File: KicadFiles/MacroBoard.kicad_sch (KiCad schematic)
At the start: 76 parts, among them J1 USB_B_Micro, J2 Conn_01x08_Male, J3 Conn_01x24_Female, SW1 SW_Push, SW10 SW_Push, SW11 SW_Push, SW12 SW_Push, SW13 RotaryEncoder_Switch, SW14 SW_Push, SW15 SW_Push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

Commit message: Add files via upload
TODO: 
add footprints
add pads for measurments
create PCB design
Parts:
- removed C27, C28, C29: 4.7u, symbol Device:C
- removed J3: Conn_01x24_Female, symbol Connector:Conn_01x24_Female
- removed U2: IFX27001TFV, Package_TO_SOT_SMD:TO-252-3_TabPin2, symbol Regulator_Linear:IFX27001TFV
- added D18: LED_RAGB, symbol Device:LED_RAGB
- added R8: 100, symbol Device:R
- added R9: 150, symbol Device:R
- added U2: TC1262-33, symbol Regulator_Linear:TC1262-33
- C25, C26: value C -> 1u
- R6: value 1M -> 100
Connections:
- net +3V3: now also U2.3 (VO)
- net +5V: now also D18.2 (A), U2.1 (VI)
- net GND: now also U2.2 (GND); no longer R6.2
- net led_blue: now reaches R6.1
- net led_blue: now also U1.31 (PA10)
- net led_green: now reaches U1.32 (PA11)
- net led_green: now also R8.1
- net CS: no longer names the net of U1.26 (PB13)
- net D/C: no longer names the net of U1.28 (PB15)
- net MISO renamed led_red
- net led_red: now also R9.1
- net MOSI: no longer names the net of U1.41 (PB5)
- net RES: no longer names the net of U1.27 (PB14)
- new net: D18.1 (RK), R9.2
- new net: D18.3 (GK), R8.2
- new net: D18.4 (BK), R6.2
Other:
- note added: "0.2"
- note added: "15.12.2022r."
- note added: "DNP"
- note added: "NOTES: - all resistors 1/4W unless specified - switch capacitors - DNP - JTAG connector for programming - DNP"
- note added: "RGB LED"
- note added: "TC1263 used"
- note added: "TODO: - footprint assignment - add pads for measurments"
- note removed: "0.1"
- note removed: "26.11.2022r."
- note removed: "OLED connector"
- note removed: "TODO: find the right voltage regulator and capacitor sizes"
- note removed: "change to the desired IC"

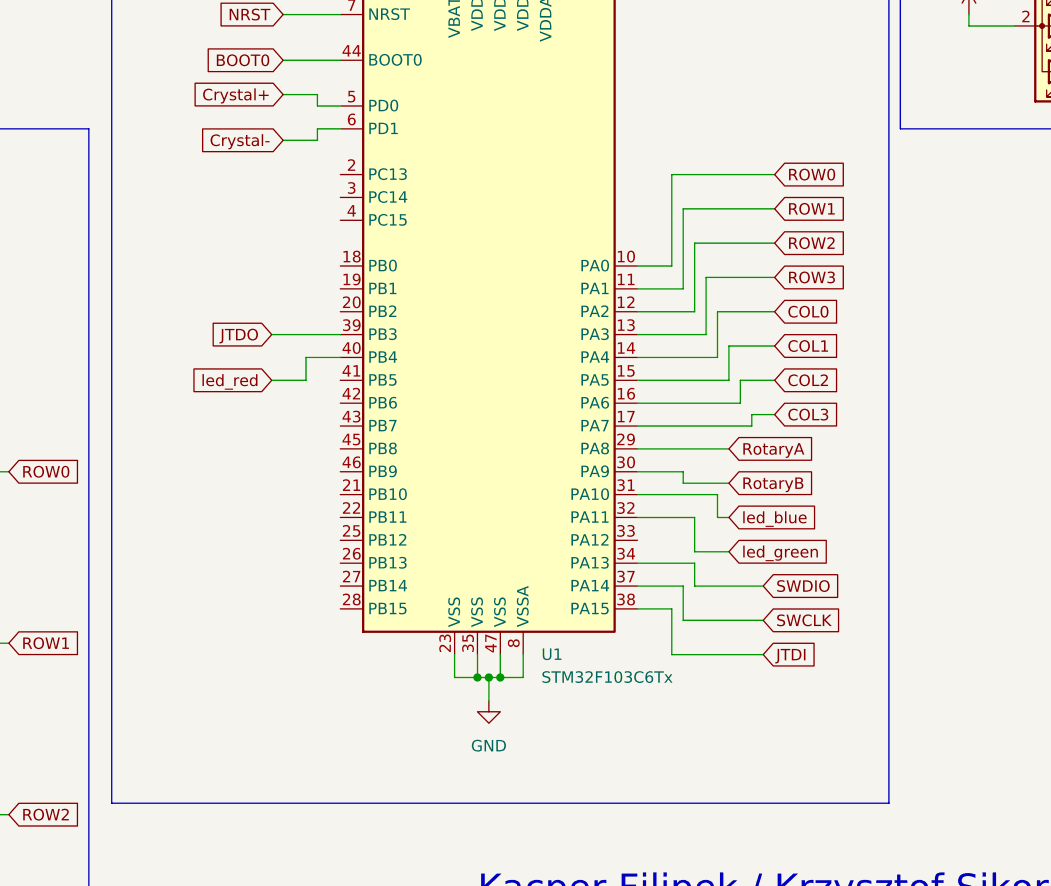
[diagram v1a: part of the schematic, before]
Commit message: Add files via upload
Pinout changes
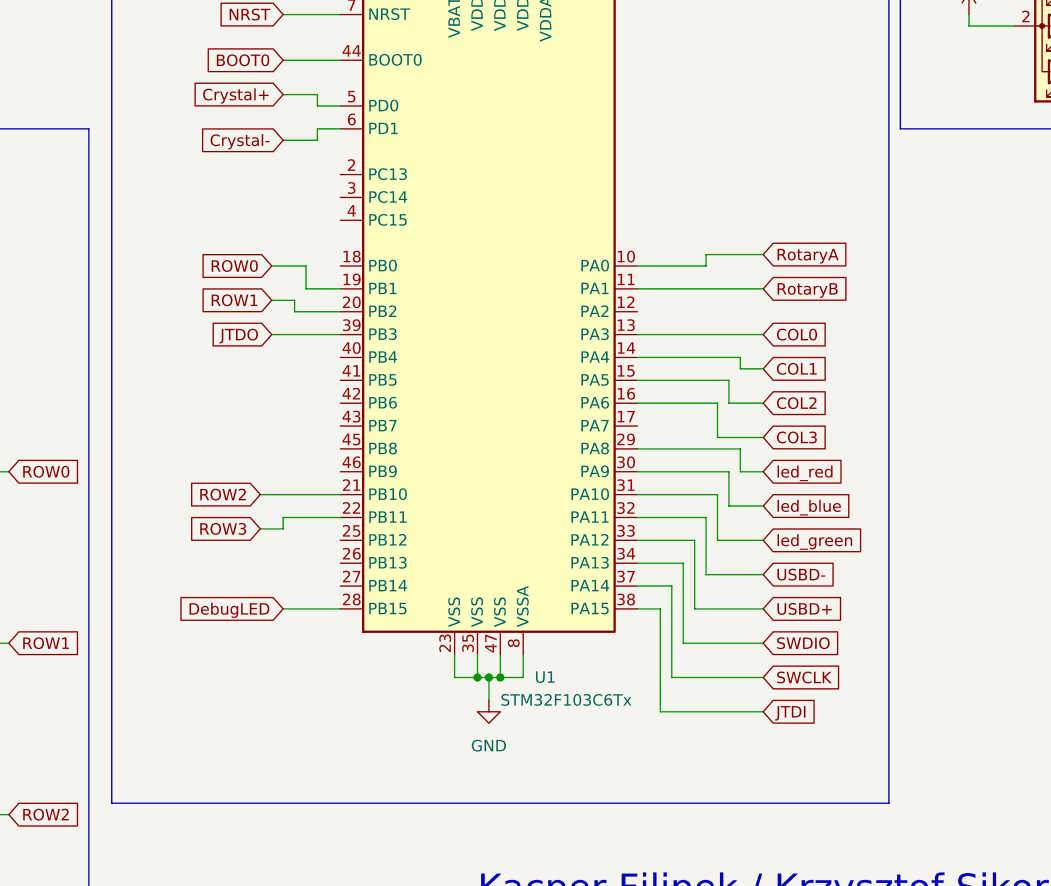
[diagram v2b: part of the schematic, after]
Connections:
- net COL0: now also U1.13 (PA3); no longer U1.14 (PA4)
- net COL1: now also U1.14 (PA4); no longer U1.15 (PA5)
- net COL2: now also U1.15 (PA5); no longer U1.16 (PA6)
- net COL3: now also U1.16 (PA6); no longer U1.17 (PA7)
- net DebugLED: now also U1.28 (PB15)
- net ROW0: now also U1.19 (PB1); no longer U1.10 (PA0)
- net ROW1: now also U1.20 (PB2); no longer U1.11 (PA1)
- net ROW2: now also U1.21 (PB10); no longer U1.12 (PA2)
- net ROW3: now also U1.22 (PB11); no longer U1.13 (PA3)
- net RotaryA: now also U1.10 (PA0); no longer U1.29 (PA8)
- net RotaryB: now also U1.11 (PA1); no longer U1.30 (PA9)
- net USBD+: now also U1.33 (PA12)
- net USBD-: now also U1.32 (PA11)
- net led_blue: now also U1.30 (PA9); no longer U1.31 (PA10)
- net led_green: now also U1.31 (PA10); no longer U1.32 (PA11)
- net led_red: now also U1.29 (PA8); no longer U1.40 (PB4)

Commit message: schematic done
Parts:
- added H1, H2, H3, H4: MountingHole, MountingHole:MountingHole_3mm, symbol Mechanical:MountingHole
- C1, C2: footprint (none) -> Capacitor_SMD:C_0603_1608Metric_Pad1.08x0.95mm_HandSolder
- C10, C11, C12, C13, C14, C15, C16, C17, C18, C19, C20, C21, C22, C23, C24, C25, C26, C3, C4, C5, C6, C7, C8, C9: footprint (none) -> Capacitor_SMD:C_0805_2012Metric_Pad1.18x1.45mm_HandSolder
- D1, D10, D11, D12, D13, D14, D15, D16, D2, D3, D4, D5, D6, D7, D8, D9: footprint (none) -> Diode_SMD:D_SOD-123F
- D17: footprint (none) -> LED_THT:LED_D5.0mm
- D18: footprint (none) -> LED_SMD:LED_SK6812_PLCC4_5.0x5.0mm_P3.2mm
- J1: footprint Connector_USB:USB_Micro-B_Molex_47346-0001 -> Connector_USB:USB_Micro-AB_Molex_47590-0001
- J2: footprint (none) -> Connector_PinHeader_2.54mm:PinHeader_1x08_P2.54mm_Horizontal
- R1, R2, R3, R4, R5, R6, R7, R8, R9: footprint (none) -> Resistor_SMD:R_1206_3216Metric_Pad1.30x1.75mm_HandSolder
- SW1, SW10, SW11, SW12, SW14, SW15, SW16, SW17, SW2, SW3, SW4, SW5, SW6, SW7, SW8, SW9: footprint (none) -> Button_Switch_Keyboard:SW_Cherry_MX_1.00u_PCB
- SW13: footprint (none) -> Rotary_Encoder:RotaryEncoder_Alps_EC11E-Switch_Vertical_H20mm
- U2: footprint (none) -> Package_SO:PowerIntegrations_SO-8
- Y1: footprint (none) -> Crystal:Crystal_SMD_HC49-SD_HandSoldering
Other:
- note added: "18.12.2022r."
- note added: "TODO: - add pads for measurments"
- note added: "keep those caps close to individual uC pins"
- note added: "mounting holes"
- note removed: "15.12.2022r."
- note removed: "TODO: - footprint assignment - add pads for measurments"
- note removed: "keep caps close to uC"

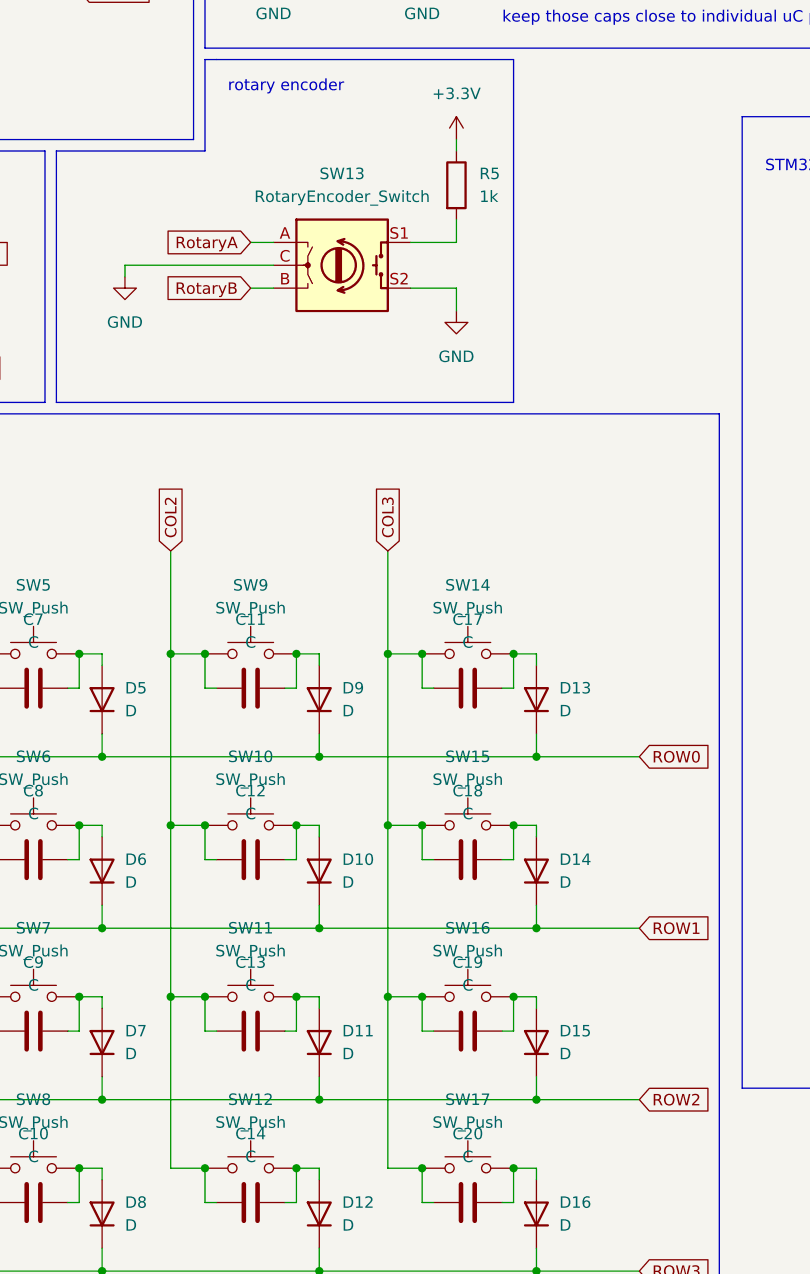
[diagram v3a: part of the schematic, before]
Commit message: pcb: arranged and connected switches with caps and diodes, everything else sucks
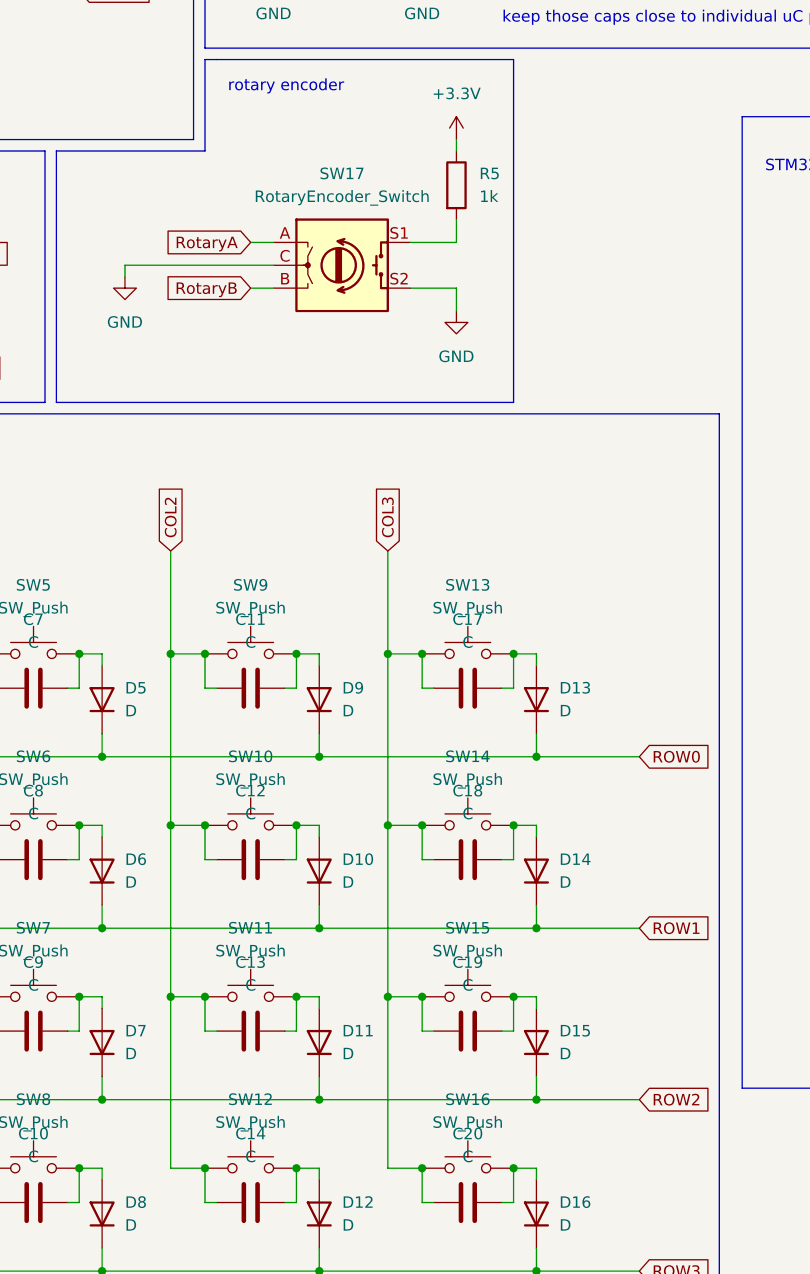
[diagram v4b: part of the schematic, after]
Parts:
- renumbered SW14 to SW13, SW15 to SW14, SW16 to SW15, SW17 to SW16, SW13 to SW17
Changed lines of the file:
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@@
   (symbol (lib_id "Switch:SW_Push") (at 106.68 111.76 0) (unit 1)
     (in_bom yes) (on_board yes) (fields_autoplaced)
-    (property "Reference" "SW14" (id 0) (at 106.68 104.14 0))
+    (property "Reference" "SW13" (id 0) (at 106.68 104.14 0))
     (property "Value" "SW_Push" (id 1) (at 106.68 106.68 0))
     (property "Footprint" "Button_Switch_Keyboard:SW_Cherry_MX_1.00u_PCB" (id 2) (at 106.68 106.68 0)
@@
   (symbol (lib_id "Switch:SW_Push") (at 106.68 149.86 0) (unit 1)
     (in_bom yes) (on_board yes) (fields_autoplaced)
-    (property "Reference" "SW16" (id 0) (at 106.68 142.24 0))
+    (property "Reference" "SW15" (id 0) (at 106.68 142.24 0))
     (property "Value" "SW_Push" (id 1) (at 106.68 144.78 0))
     (property "Footprint" "Button_Switch_Keyboard:SW_Cherry_MX_1.00u_PCB" (id 2) (at 106.68 144.78 0)
@@
   (symbol (lib_id "Switch:SW_Push") (at 106.68 168.91 0) (unit 1)
     (in_bom yes) (on_board yes) (fields_autoplaced)
-    (property "Reference" "SW17" (id 0) (at 106.68 161.29 0))
+    (property "Reference" "SW16" (id 0) (at 106.68 161.29 0))
     (property "Value" "SW_Push" (id 1) (at 106.68 163.83 0))
     (property "Footprint" "Button_Switch_Keyboard:SW_Cherry_MX_1.00u_PCB" (id 2) (at 106.68 163.83 0)
@@
   (symbol (lib_id "Device:RotaryEncoder_Switch") (at 92.71 68.58 0) (unit 1)
     (in_bom yes) (on_board yes)
-    (property "Reference" "SW13" (id 0) (at 92.71 58.42 0))
+    (property "Reference" "SW17" (id 0) (at 92.71 58.42 0))
     (property "Value" "RotaryEncoder_Switch" (id 1) (at 92.71 60.96 0))
     (property "Footprint" "Rotary_Encoder:RotaryEncoder_Alps_EC11E-Switch_Vertical_H20mm" (id 2) (at 88.9 64.516 0)
@@
   (symbol (lib_id "Switch:SW_Push") (at 106.68 130.81 0) (unit 1)
     (in_bom yes) (on_board yes) (fields_autoplaced)
-    (property "Reference" "SW15" (id 0) (at 106.68 123.19 0))
+    (property "Reference" "SW14" (id 0) (at 106.68 123.19 0))
     (property "Value" "SW_Push" (id 1) (at 106.68 125.73 0))
     (property "Footprint" "Button_Switch_Keyboard:SW_Cherry_MX_1.00u_PCB" (id 2) (at 106.68 125.73 0)
@@
       (reference "SW12") (unit 1) (value "SW_Push") (footprint "Button_Switch_Keyboard:SW_Cherry_MX_1.00u_PCB")
     )
+    (path "/3ff120d4-f1ea-4811-aff9-4befd8200d1d"
+      (reference "SW13") (unit 1) (value "SW_Push") (footprint "Button_Switch_Keyboard:SW_Cherry_MX_1.00u_PCB")
+    )
+    (path "/fda4341c-de17-4e4e-af84-4ddb55431f64"
+      (reference "SW14") (unit 1) (value "SW_Push") (footprint "Button_Switch_Keyboard:SW_Cherry_MX_1.00u_PCB")
+    )
+    (path "/476e003f-c1f1-473f-bc74-54dfd09b7a8a"
+      (reference "SW15") (unit 1) (value "SW_Push") (footprint "Button_Switch_Keyboard:SW_Cherry_MX_1.00u_PCB")
+    )
+    (path "/53a5589d-91cb-4e11-96fa-311b69a13e42"
+      (reference "SW16") (unit 1) (value "SW_Push") (footprint "Button_Switch_Keyboard:SW_Cherry_MX_1.00u_PCB")
+    )
     (path "/e77f1d56-c211-430d-accf-66e21b6abde1"
-      (reference "SW13") (unit 1) (value "RotaryEncoder_Switch") (footprint "Rotary_Encoder:RotaryEncoder_Alps_EC11E-Switch_Vertical_H20mm")
-    )
-    (path "/3ff120d4-f1ea-4811-aff9-4befd8200d1d"
-      (reference "SW14") (unit 1) (value "SW_Push") (footprint "Button_Switch_Keyboard:SW_Cherry_MX_1.00u_PCB")
-    )
-    (path "/fda4341c-de17-4e4e-af84-4ddb55431f64"
-      (reference "SW15") (unit 1) (value "SW_Push") (footprint "Button_Switch_Keyboard:SW_Cherry_MX_1.00u_PCB")
-    )
-    (path "/476e003f-c1f1-473f-bc74-54dfd09b7a8a"
-      (reference "SW16") (unit 1) (value "SW_Push") (footprint "Button_Switch_Keyboard:SW_Cherry_MX_1.00u_PCB")
-    )
-    (path "/53a5589d-91cb-4e11-96fa-311b69a13e42"
-      (reference "SW17") (unit 1) (value "SW_Push") (footprint "Button_Switch_Keyboard:SW_Cherry_MX_1.00u_PCB")
+      (reference "SW17") (unit 1) (value "RotaryEncoder_Switch") (footprint "Rotary_Encoder:RotaryEncoder_Alps_EC11E-Switch_Vertical_H20mm")
     )
     (path "/e3fcbf5e-ef0b-42f1-a0b5-f37d0a27f3c9"
